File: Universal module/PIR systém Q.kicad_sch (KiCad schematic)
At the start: 37 parts, among them J2 PIR, J3 BUS, J4 Conn_01x04_Socket, J5 USB_B_Mini, Q1 BC846, Q2 BC846, Q3 BC857, SW1 tamper switch, U1 AP63203WU, U2 WT8266-S1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

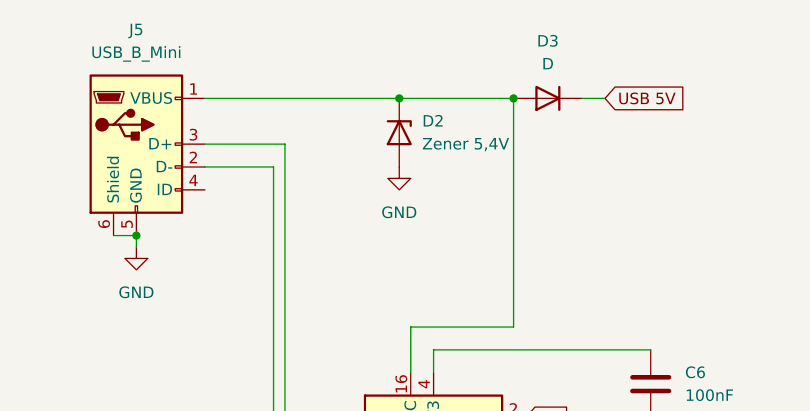
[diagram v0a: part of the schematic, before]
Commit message: better diode
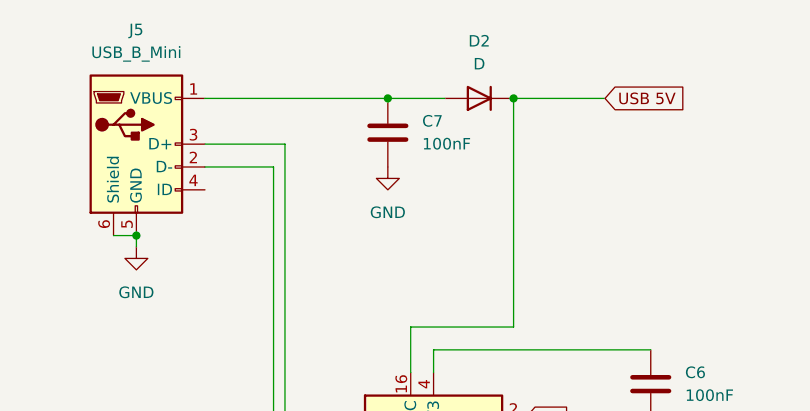
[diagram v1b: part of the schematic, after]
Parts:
- removed D2: Zener 5,4V, symbol Device:D_Zener
- removed D3: D, symbol Device:D
- added C7: 100nF, symbol Device:C
- added D2: D, symbol Device:D
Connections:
- net +12V: now also U3.16 (VCC), D2.1 (K)
- net GND: now also C7.2
- net at J5.1 (VBUS): now also C7.1, D2.2 (A); no longer U3.16 (VCC)

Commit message: add features
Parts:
- removed J2: PIR, Connector_PinSocket_2.54mm:PinSocket_1x03_P2.54mm_Vertical, symbol Connector:Conn_01x03_Pin
- removed J3: BUS, TerminalBlock:TerminalBlock_Altech_AK300-4_P5.00mm, symbol Connector:Screw_Terminal_01x04
- added J1: Screw_Terminal_01x06, symbol Connector:Screw_Terminal_01x06
- added Q4, Q5: BC817, Package_TO_SOT_SMD:SOT-23, symbol Transistor_BJT:BC817
- added R8, R9: R, symbol Device:R
- added U4: P82B96, symbol Interface_Expansion:P82B96
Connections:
- net +12V: now also U4.8 (VCC)
- net +3.3V: now also J1.5 (Pin_5)
- net GND: now also J1.2 (Pin_2), U4.4 (GND)
- net GPIO0: now also Q5.2 (E)
- net I2C data: now also U4.1 (SDA)
- net PIR signal: no longer TP1.1
- net clock: now also U4.7 (SCL)
- net at D4.2 (A): now also J1.1 (Pin_1)
- net at U3.14 (~{RTS}): now also Q4.2 (E), R9.1
- net "reset" renamed ESP_EN
- net ESP_EN: now also Q4.3 (C); no longer U3.13 (~{DTR})
- new net: Q5.3 (C), R8.1, U3.13 (~{DTR})
- new net: Q4.1 (B), R8.2
- new net: Q5.1 (B), R9.2
- new net PIR Signal: J1.6 (Pin_6), TP1.1
- new net SCL: J1.4 (Pin_4), U4.5 (TXD-SCL), U4.6 (RXD-SCL)
- new net SDA: J1.3 (Pin_3), U4.2 (RXD-SDA), U4.3 (TXD-SDA)
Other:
- moved on the sheet: C5, D1, D4, R4, R5, TP5, U2

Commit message: better design
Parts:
- added R10, R11: 10k, symbol Device:R
- R8, R9: value R -> 10k
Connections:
- net +12V: no longer U3.16 (VCC)
- net +3.3V: now also C6.1, U3.16 (VCC), U3.4 (V3), R10.1, R11.1; no longer R7.1
- net GND: now also R7.2
- net GPIO0: now also R7.1; no longer R7.2
- net I2C data: now also R10.2
- net clock: now also R11.2
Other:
- moved on the sheet: C7, D2, J5, Q4, Q5, R8, R9, U3, U4

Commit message: begun the drawing of the PCB, fixed libraries
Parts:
- removed R7: 10k, Resistor_SMD:R_0603_1608Metric, symbol Device:R
- added R12: 10k, Resistor_SMD:R_0603_1608Metric, symbol Device:R
- BZ1: footprint LPT2270AS buzzer:LPT2270AS -> piezo:LPT2270AS
- C6, C7: footprint (none) -> Capacitor_SMD:C_0603_1608Metric
- D2, D4: footprint (none) -> Diode_SMD:D_0603_1608Metric
- J1: footprint (none) -> TerminalBlock_Phoenix:TerminalBlock_Phoenix_MKDS-1,5-6_1x06_P5.00mm_Horizontal
- J5: footprint (none) -> Connector_USB:USB_Mini-B_Tensility_54-00023_Vertical
- R10, R11, R8, R9: footprint (none) -> Resistor_SMD:R_0603_1608Metric
- U4: footprint (none) -> P82B96D:SOIC127P599X175-8N
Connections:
- net +3.3V: now also R12.1
- net GPIO0: now also Q5.3 (C), R12.2; no longer Q5.2 (E)
- net at R8.1, U3.13 (~{DTR}): now also Q5.2 (E); no longer Q5.3 (C)
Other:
- moved on the sheet: Q4, Q5, R8, R9

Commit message: basic PCB design
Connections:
- net PIR signal is gone; now on net PIR Signal: U2.2 (GPIO4)

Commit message: finish PCB design, bonus gerber files
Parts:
- removed TP1: 3,3V, TestPoint:TestPoint_Pad_1.5x1.5mm, symbol Connector:TestPoint
- added keyboard_exp1: Conn_01x04_Socket, Connector_PinSocket_2.54mm:PinSocket_1x04_P2.54mm_Vertical, symbol Connector:Conn_01x04_Socket
- BZ1: value Buzzer -> Siren
- J4: footprint Connector_PinSocket_2.54mm:PinSocket_1x04_P2.54mm_Horizontal -> Connector_PinSocket_2.54mm:PinSocket_1x04_P2.54mm_Vertical
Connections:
- net GPIO0: now also keyboard_exp1.2 (Pin_2)
- net PIR Signal: now also keyboard_exp1.1 (Pin_1)
- net RX: now also keyboard_exp1.4 (Pin_4)
- net TX: now also keyboard_exp1.3 (Pin_3)
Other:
- company: Radim Kolář, Tomáš Bezányi -> Radim Kolář
- title: Q PIR -> EZS Q - Universal module
- moved on the sheet: TP3
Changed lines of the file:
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@@
 	(paper "A3")
 	(title_block
-		(title "Q PIR")
+		(title "EZS Q - Universal module")
 		(rev "5")
-		(company "Radim Kolář, Tomáš Bezányi")
+		(company "Radim Kolář")
 	)
 	(junction
@@
 	)
 	(junction
-		(at 63.5 222.25)
-		(diameter 0)
-		(color 0 0 0 0)
-	)
-	(junction
 		(at 247.65 236.22)
 		(diameter 0)
@@
 	(wire
 		(pts
+			(xy 195.58 201.93) (xy 195.58 198.12)
+		)
+		(stroke
+			(width 0)
+			(type default)
+		)
+	)
+	(wire
+		(pts
 			(xy 49.53 50.8) (xy 52.07 50.8)
 		)
@@
 	(wire
 		(pts
-			(xy 63.5 222.25) (xy 63.5 217.17)
+			(xy 63.5 217.17) (xy 63.5 224.79)
 		)
 		(stroke
@@
 	(wire
 		(pts
-			(xy 63.5 224.79) (xy 63.5 222.25)
-		)
-		(stroke
-			(width 0)
-			(type default)
-		)
-	)
-	(wire
-		(pts
 			(xy 114.3 151.13) (xy 114.3 153.67)
 		)
@@
 		)
 	)
+	(global_label "RX"
+		(shape input)
+		(at 312.42 82.55 180)
+		(fields_autoplaced yes)
+		(effects
+			(font
+				(size 1.27 1.27)
+			)
+			(justify right)
+		)
+		(property "Intersheetrefs" "${INTERSHEET_REFS}"
+			(at 306.9553 82.55 0)
+			(effects
+				(font
+					(size 1.27 1.27)
+				)
+				(justify right)
+				(hide yes)
+			)
+		)
+	)
 	(global_label "TX"
 		(shape input)
@@
 		)
 	)
+	(global_label "GPIO0"
+		(shape input)
+		(at 312.42 77.47 180)
+		(fields_autoplaced yes)
+		(effects
+			(font
+				(size 1.27 1.27)
+			)
+			(justify right)
+		)
+		(property "Intersheetrefs" "${INTERSHEET_REFS}"
+			(at 303.75 77.47 0)
+			(effects
+				(font
+					(size 1.27 1.27)
+				)
+				(justify right)
+				(hide yes)
+			)
+		)
+	)
 	(global_label "battery voltage"
 		(shape input)
@@
 		)
 	)
+	(global_label "PIR Signal"
+		(shape input)
+		(at 312.42 74.93 180)
+		(fields_autoplaced yes)
+		(effects
+			(font
+				(size 1.27 1.27)
+			)
+			(justify right)
+		)
+		(property "Intersheetrefs" "${INTERSHEET_REFS}"
+			(at 299.3959 74.93 0)
+			(effects
+				(font
+					(size 1.27 1.27)
+				)
+				(justify right)
+				(hide yes)
+			)
+		)
+	)
 	(global_label "battery voltage"
 		(shape input)
@@
 		)
 	)
+	(global_label "TX"
+		(shape input)
+		(at 312.42 80.01 180)
+		(fields_autoplaced yes)
+		(effects
+			(font
+				(size 1.27 1.27)
+			)
+			(justify right)
+		)
+		(property "Intersheetrefs" "${INTERSHEET_REFS}"
+			(at 307.2577 80.01 0)
+			(effects
+				(font
+					(size 1.27 1.27)
+				)
+				(justify right)
+				(hide yes)
+			)
+		)
+	)
 	(global_label "GPIO0"
 		(shape input)
@@
 	)
 	(symbol
+		(lib_id "Connector:Conn_01x04_Socket")
+		(at 317.5 77.47 0)
+		(unit 1)
+		(exclude_from_sim no)
+		(in_bom yes)
+		(on_board yes)
+		(dnp no)
+		(fields_autoplaced yes)
+		(property "Reference" "keyboard_exp1"
+			(at 318.77 77.4699 0)
+			(effects
+				(font
+					(size 1.27 1.27)
+				)
+				(justify left)
+			)
+		)
+		(property "Value" "Conn_01x04_Socket"
+			(at 318.77 80.0099 0)
+			(effects
+				(font
+					(size 1.27 1.27)
+				)
+				(justify left)
+			)
+		)
+		(property "Footprint" "Connector_PinSocket_2.54mm:PinSocket_1x04_P2.54mm_Vertical"
+			(at 317.5 77.47 0)
+			(effects
+				(font
+					(size 1.27 1.27)
+				)
+				(hide yes)
+			)
+		)
+		(property "Datasheet" "~"
+			(at 317.5 77.47 0)
+			(effects
+				(font
+					(size 1.27 1.27)
+				)
+				(hide yes)
+			)
+		)
+		(property "Description" ""
+			(at 317.5 77.47 0)
+			(effects
+				(font
+					(size 1.27 1.27)
+				)
+				(hide yes)
+			)
+		)
+		(pin "1"
+		)
+		(pin "2"
+		)
+		(pin "3"
+		)
+		(pin "4"
+		)
+		(instances
+			(project "PIR systém Q"
+				(path "/bd84660b-13bb-4554-9f23-8e30376967c6"
+					(reference "keyboard_exp1")
+					(unit 1)
+				)
+			)
+		)
+	)
+	(symbol
 		(lib_name "+3.3V_1")
 		(lib_id "power:+3.3V")
@@
 			)
 		)
-		(property "Footprint" "Connector_PinSocket_2.54mm:PinSocket_1x04_P2.54mm_Horizontal"
+		(property "Footprint" "Connector_PinSocket_2.54mm:PinSocket_1x04_P2.54mm_Vertical"
 			(at 321.31 153.67 0)
 			(effects
@@
 		(fields_autoplaced yes)
 		(property "Reference" "BZ1"
-			(at 280.67 241.3 0)
+			(at 280.67 241.2999 0)
 			(effects
 				(font
@@
 			)
 		)
-		(property "Value" "Buzzer"
-			(at 280.67 243.84 0)
+		(property "Value" "Siren"
+			(at 280.67 243.8399 0)
 			(effects
 				(font
@@
 	(symbol
 		(lib_id "Connector:TestPoint")
-		(at 63.5 222.25 270)
-		(unit 1)
-		(exclude_from_sim no)
-		(in_bom yes)
-		(on_board yes)
-		(dnp no)
-		(fields_autoplaced yes)
-		(property "Reference" "TP1"
-			(at 68.58 220.9799 90)
-			(effects
-				(font
-					(size 1.27 1.27)
-				)
-				(justify left)
-			)
-		)
-		(property "Value" "3,3V"
-			(at 68.58 223.5199 90)
-			(effects
-				(font
-					(size 1.27 1.27)
-				)
-				(justify left)
-			)
-		)
-		(property "Footprint" "TestPoint:TestPoint_Pad_1.5x1.5mm"
-			(at 63.5 227.33 0)
-			(effects
-				(font
-					(size 1.27 1.27)
-				)
-				(hide yes)
-			)
-		)
-		(property "Datasheet" "~"
-			(at 63.5 227.33 0)
-			(effects
-				(font
-					(size 1.27 1.27)
-				)
-				(hide yes)
-			)
-		)
-		(property "Description" ""
-			(at 63.5 222.25 0)
-			(effects
-				(font
-					(size 1.27 1.27)
-				)
-				(hide yes)
-			)
-		)
-		(pin "1"
-		)
-		(instances
-			(project "PIR systém Q"
-				(path "/bd84660b-13bb-4554-9f23-8e30376967c6"
-					(reference "TP1")
-					(unit 1)
-				)
-			)
-		)
-	)
-	(symbol
-		(lib_id "Connector:TestPoint")
-		(at 195.58 198.12 180)
+		(at 195.58 201.93 180)
 		(unit 1)
 		(exclude_from_sim no)
@@
 		(dnp no)
 		(property "Reference" "TP3"
-			(at 187.96 198.12 0)
+			(at 187.96 201.93 0)
 			(effects
 				(font
@@
 		)
 		(property "Value" "12V"
-			(at 187.96 200.66 0)
+			(at 187.96 204.47 0)
 			(effects
 				(font
@@
 		)
 		(property "Footprint" "TestPoint:TestPoint_Pad_1.5x1.5mm"
-			(at 190.5 198.12 0)
+			(at 190.5 201.93 0)
 			(effects
 				(font
@@
 		)
 		(property "Datasheet" "~"
-			(at 190.5 198.12 0)
+			(at 190.5 201.93 0)
 			(effects
 				(font
@@
 		)
 		(property "Description" ""
-			(at 195.58 198.12 0)
+			(at 195.58 201.93 0)
 			(effects
 				(font
